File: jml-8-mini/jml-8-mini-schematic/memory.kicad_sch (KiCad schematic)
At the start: 3 parts, among them U2 28HC64, U3 60L256

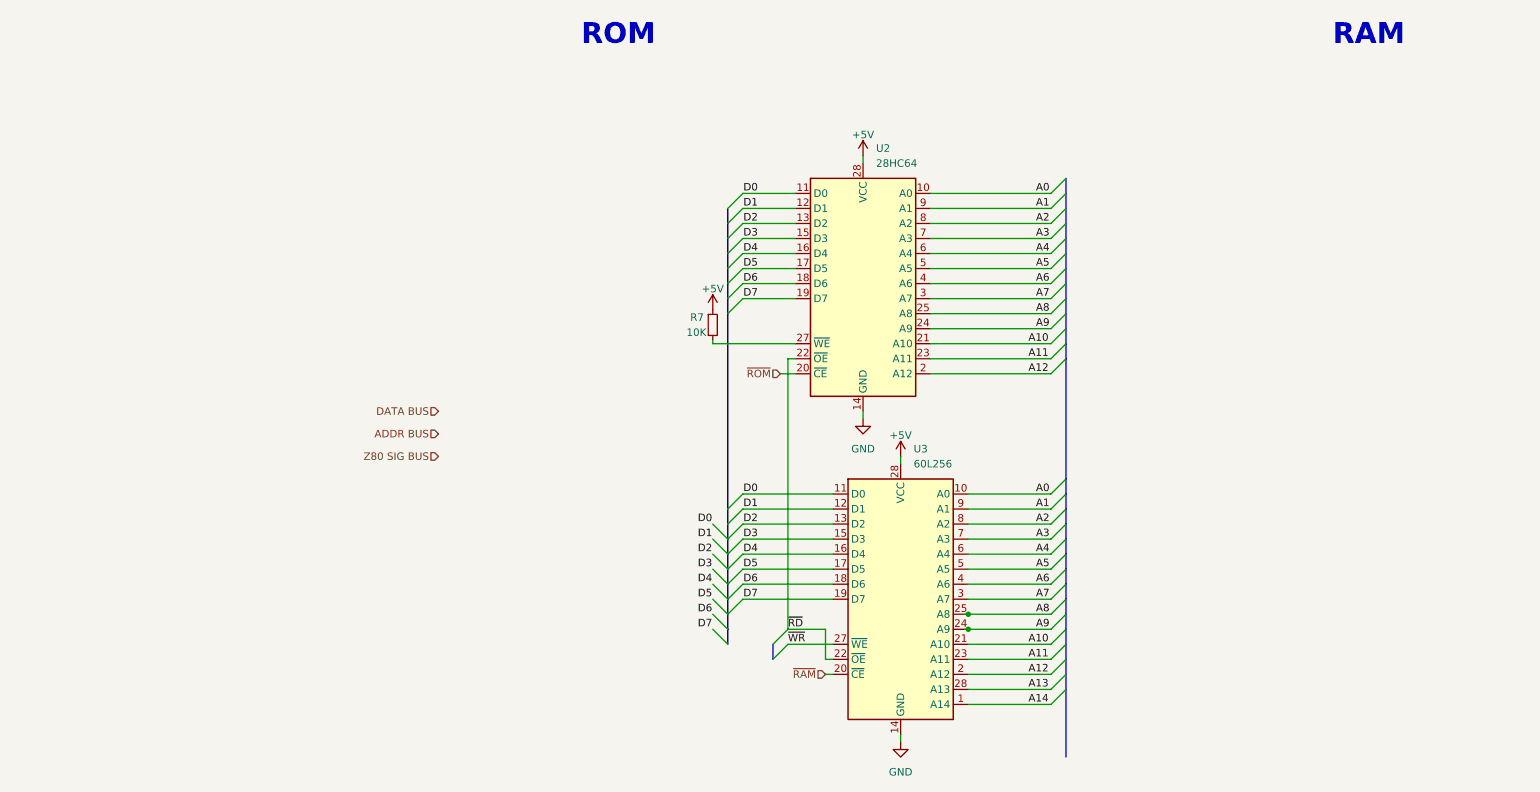
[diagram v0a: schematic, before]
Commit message: lots of changes to schematic, redone to make easier to read and add to
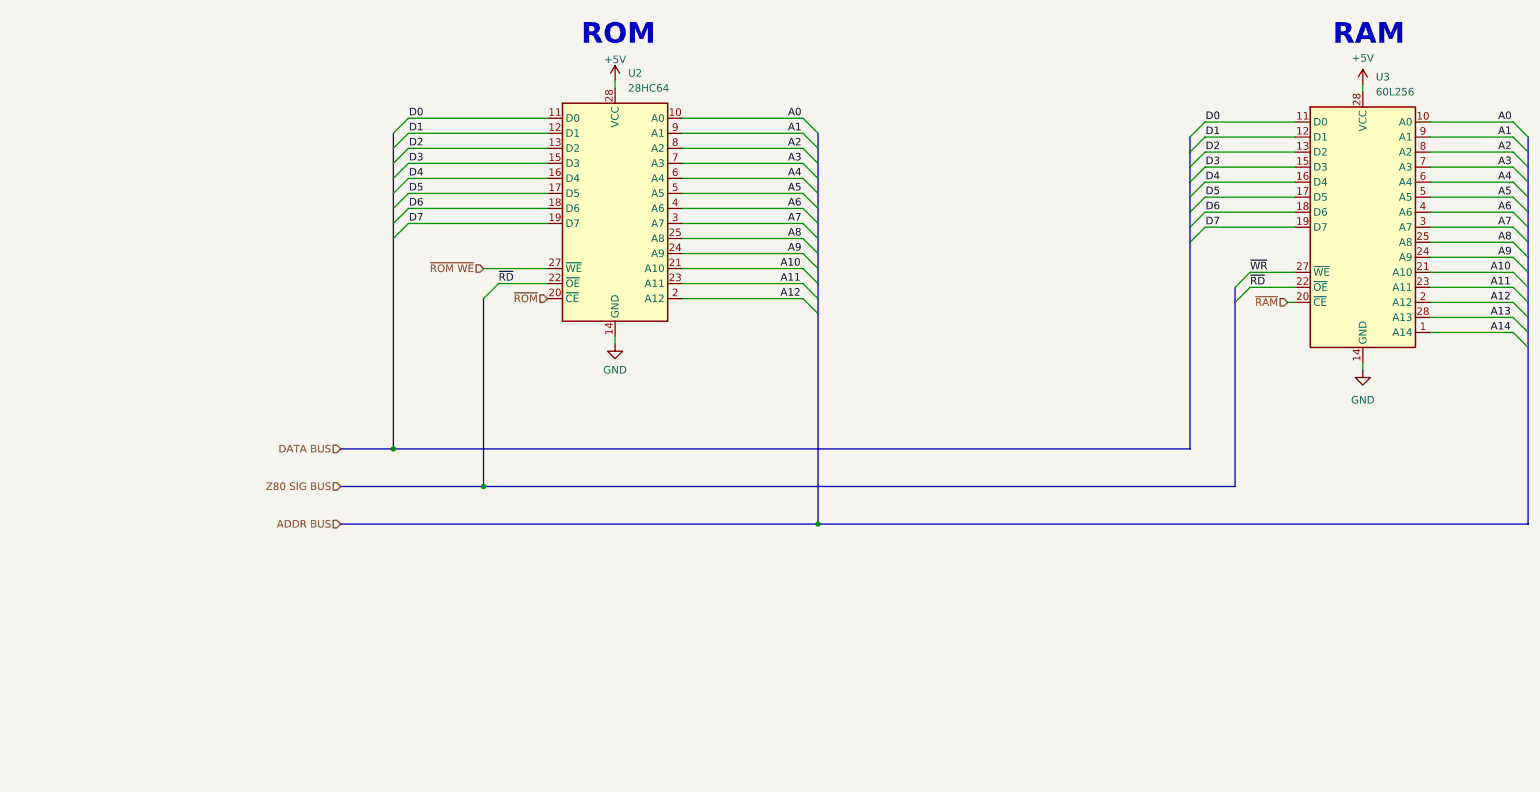
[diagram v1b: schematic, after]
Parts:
- removed R7: 10K, symbol Device:R_Small
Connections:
- net ~{ROM WE}: now reaches U2.27 (~{WE})
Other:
- moved on the sheet: U2, U3

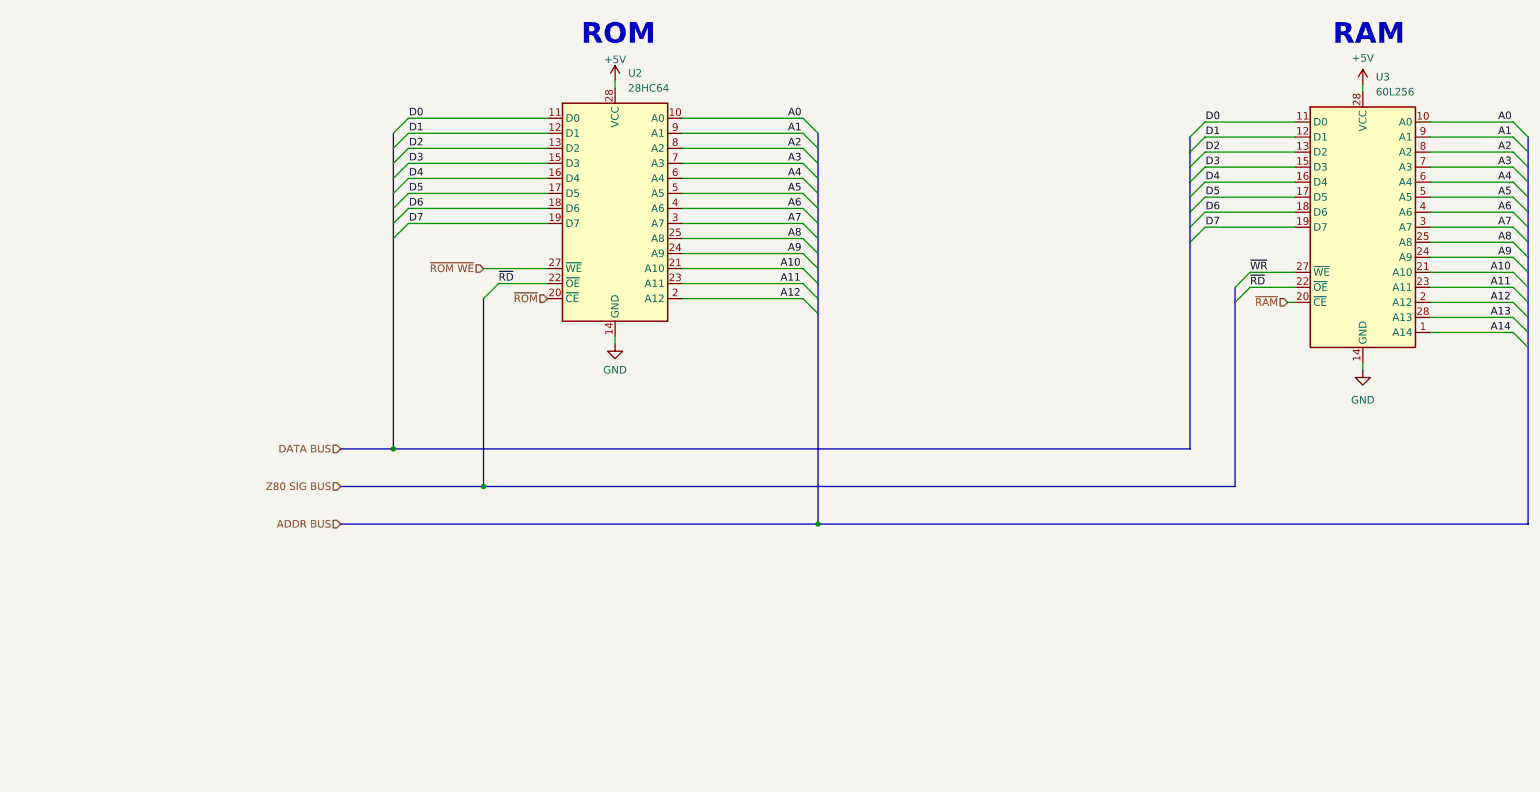
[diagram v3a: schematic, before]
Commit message: complete schematic
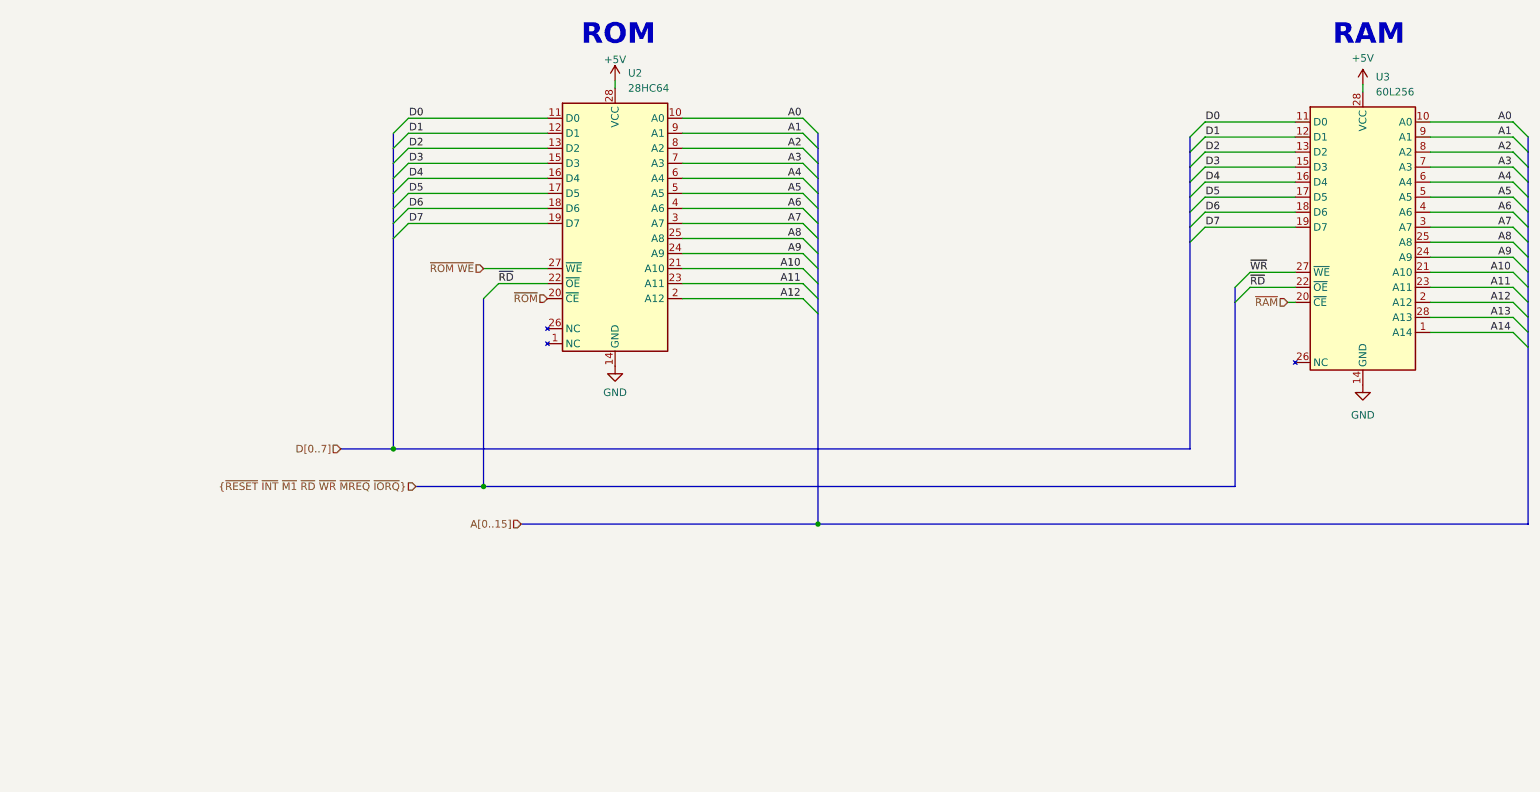
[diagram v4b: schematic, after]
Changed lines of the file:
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@@
 (kicad_sch (version 20230121) (generator eeschema)
   (paper "A4")
+  (title_block
+    (date "2023-10-02")
+    (rev "A")
+    (comment 1 "Author: Jacob Long")
+  )
   (junction (at 118.745 107.95) (diameter 0) (color 0 0 0 0)
   )
@@
     (stroke (width 0) (type default))
   )
-  (bus (pts (xy 38.1 107.95) (xy 118.745 107.95))
+  (bus (pts (xy 68.58 107.95) (xy 118.745 107.95))
     (stroke (width 0) (type default))
   )
@@
     (stroke (width 0) (type default))
   )
-  (wire (pts (xy 210.82 80.645) (xy 210.82 81.915))
-    (stroke (width 0) (type default))
-  )
   (wire (pts (xy 222.25 70.485) (xy 236.22 70.485))
     (stroke (width 0) (type default))
@@
     (stroke (width 0) (type default))
   )
-  (wire (pts (xy 84.455 76.2) (xy 84.455 77.47))
-    (stroke (width 0) (type default))
-  )
   (bus (pts (xy 118.745 72.39) (xy 118.745 107.95))
     (stroke (width 0) (type default))
@@
     (stroke (width 0) (type default))
   )
-  (bus (pts (xy 38.1 101.6) (xy 62.23 101.6))
+  (bus (pts (xy 50.8 101.6) (xy 62.23 101.6))
     (stroke (width 0) (type default))
   )
@@
     (effects (font (size 1.27 1.27)) (justify right bottom))
   )
-  (hierarchical_label "ADDR BUS" (shape input) (at 38.1 107.95 180) (fields_autoplaced)
+  (hierarchical_label "A[0..15]" (shape input) (at 68.58 107.95 180) (fields_autoplaced)
     (effects (font (size 1.27 1.27)) (justify right))
   )
-  (hierarchical_label "DATA BUS" (shape input) (at 38.1 95.25 180) (fields_autoplaced)
+  (hierarchical_label "D[0..7]" (shape input) (at 38.1 95.25 180) (fields_autoplaced)
     (effects (font (size 1.27 1.27)) (justify right))
   )
@@
     (effects (font (size 1.27 1.27)) (justify right))
   )
-  (hierarchical_label "Z80 SIG BUS" (shape input) (at 38.1 101.6 180) (fields_autoplaced)
+  (hierarchical_label "{~{RESET} ~{INT} ~{M1} ~{RD} ~{WR} ~{MREQ} ~{IORQ}}" (shape input)
+    (at 50.8 101.6 180) (fields_autoplaced)
     (effects (font (size 1.27 1.27)) (justify right))
   )
@@
     )
   )
-  (symbol (lib_id "power:GND") (at 210.82 81.915 0) (unit 1)
+  (symbol (lib_id "power:GND") (at 210.82 84.455 0) (unit 1)
     (in_bom yes) (on_board yes) (dnp no) (fields_autoplaced)
-    (property "Reference" "#PWR09" (at 210.82 88.265 0)
-      (effects (font (size 1.27 1.27)) hide)
-    )
-    (property "Value" "GND" (at 210.82 86.995 0)
+    (property "Reference" "#PWR09" (at 210.82 90.805 0)
+      (effects (font (size 1.27 1.27)) hide)
+    )
+    (property "Value" "GND" (at 210.82 89.535 0)
       (effects (font (size 1.27 1.27)))
     )
-    (property "Footprint" "" (at 210.82 81.915 0)
-      (effects (font (size 1.27 1.27)) hide)
-    )
-    (property "Datasheet" "" (at 210.82 81.915 0)
+    (property "Footprint" "" (at 210.82 84.455 0)
+      (effects (font (size 1.27 1.27)) hide)
+    )
+    (property "Datasheet" "" (at 210.82 84.455 0)
       (effects (font (size 1.27 1.27)) hide)
     )
@@
     )
   )
-  (symbol (lib_name "MCM60L256AP85_1") (lib_id "jml-8-mini-library:MCM60L256AP85") (at 210.82 57.785 0) (unit 1)
+  (symbol (lib_id "jml-8-mini-library:MCM60L256AP85") (at 210.82 57.785 0) (unit 1)
     (in_bom yes) (on_board yes) (dnp no) (fields_autoplaced)
     (property "Reference" "U3" (at 213.0141 32.385 0)
@@
     (pin "24")
     (pin "25")
+    (pin "26")
     (pin "27")
     (pin "28")
@@
     )
   )
-  (symbol (lib_id "power:GND") (at 84.455 77.47 0) (unit 1)
+  (symbol (lib_id "power:GND") (at 84.455 81.28 0) (unit 1)
     (in_bom yes) (on_board yes) (dnp no)
-    (property "Reference" "#PWR012" (at 84.455 83.82 0)
-      (effects (font (size 1.27 1.27)) hide)
-    )
-    (property "Value" "GND" (at 84.455 81.915 0)
+    (property "Reference" "#PWR012" (at 84.455 87.63 0)
+      (effects (font (size 1.27 1.27)) hide)
+    )
+    (property "Value" "GND" (at 84.455 85.725 0)
       (effects (font (size 1.27 1.27)))
     )
-    (property "Footprint" "" (at 84.455 77.47 0)
-      (effects (font (size 1.27 1.27)) hide)
-    )
-    (property "Datasheet" "" (at 84.455 77.47 0)
+    (property "Footprint" "" (at 84.455 81.28 0)
+      (effects (font (size 1.27 1.27)) hide)
+    )
+    (property "Datasheet" "" (at 84.455 81.28 0)
       (effects (font (size 1.27 1.27)) hide)
     )
@@
       (effects (font (size 1.27 1.27)) hide)
     )
+    (pin "1")
     (pin "10")
     (pin "11")
@@
     (pin "24")
     (pin "25")
+    (pin "26")
     (pin "27")
     (pin "28")

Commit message: add to info section of schematic
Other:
- company: (none) -> https://github.com/jac-oblong/jml
- title: (none) -> JML-8 Mini Schematic
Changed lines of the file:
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@@
   (paper "A4")
   (title_block
+    (title "JML-8 Mini Schematic")
     (date "2023-10-02")
     (rev "A")
-    (comment 1 "Author: Jacob Long")
+    (company "https://github.com/jac-oblong/jml")
+    (comment 1 "Design of Z80 based microcomputer")
+    (comment 3 "Released under MIT License")
+    (comment 4 "Created by: Jacob Long (https://github.com/jac-oblong)")
   )
   (junction (at 118.745 107.95) (diameter 0) (color 0 0 0 0)

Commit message: update info section of schematic
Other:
- company: https://github.com/jac-oblong/jml -> https://github.com/jac-oblong/JML
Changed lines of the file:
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@@
     (date "2023-10-02")
     (rev "A")
-    (company "https://github.com/jac-oblong/jml")
+    (company "https://github.com/jac-oblong/JML")
     (comment 1 "Design of Z80 based microcomputer")
     (comment 3 "Released under MIT License")

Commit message: change some footprints
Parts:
- U2, U3: footprint Package_DIP:DIP-28_W15.24mm_LongPads -> Package_DIP:DIP-28_W15.24mm_Socket_LongPads
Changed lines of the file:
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@@
       (effects (font (size 1.27 1.27)) (justify left))
     )
-    (property "Footprint" "Package_DIP:DIP-28_W15.24mm_LongPads" (at 210.82 55.245 0)
+    (property "Footprint" "Package_DIP:DIP-28_W15.24mm_Socket_LongPads" (at 210.82 55.245 0)
       (effects (font (size 1.27 1.27)) hide)
     )
@@
       (effects (font (size 1.27 1.27)) (justify left))
     )
-    (property "Footprint" "Package_DIP:DIP-28_W15.24mm_LongPads" (at 89.535 62.23 0)
+    (property "Footprint" "Package_DIP:DIP-28_W15.24mm_Socket_LongPads" (at 89.535 62.23 0)
       (effects (font (size 1.27 1.27)) hide)
     )
